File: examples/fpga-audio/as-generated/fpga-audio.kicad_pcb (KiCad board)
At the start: 2 copper layers, 100 x 84 mm, 29 parts, among them J1 3V3 IN, J2 AUDIO OUT, J3 SPI PROG, U1 iCE40UP5K, U2 PCM5102A, U3 AP2112K-1.2, U4 W25Q32JV, X1 12MHz

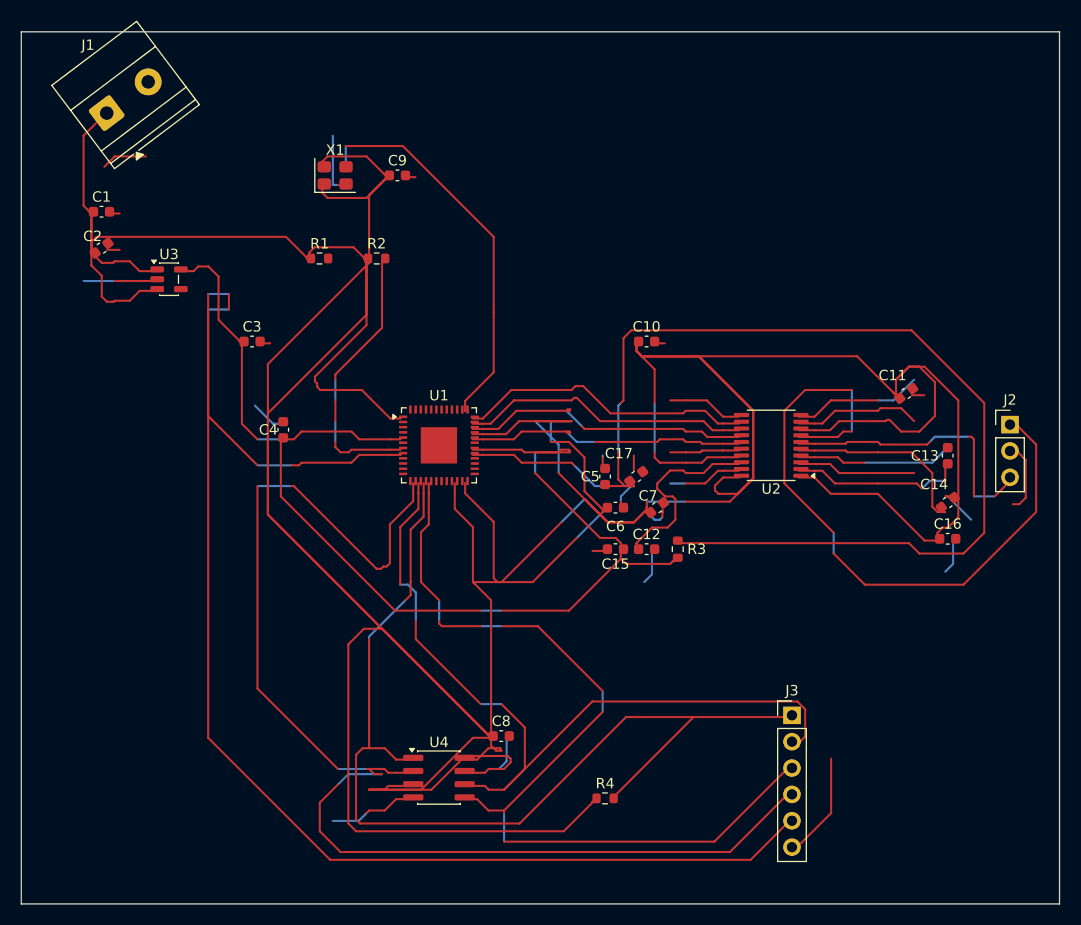
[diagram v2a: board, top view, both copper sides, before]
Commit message: Reroute the FPGA board and record what the rip-up loop bought
Eleven rip-ups and three re-orderings later, and the sixth promotion rolled
back because it left I2S_SCK with no lane:

  route.detour   VCCPLL at 5.0x   ->  gone
  route.wander   4 runs           ->  2
  acute corners  3                ->  2
  route.return_path 7 nets        ->  6
  DRC errors     1 unconnected    ->  0

Board findings 1/10/8 -> 0/9/8, and the gate goes from 5 blocking to 3. Under
KiCad's own checks the board is now clean: no DRC errors, nothing unconnected,
no schematic-parity findings.

What is left is the two-layer choice itself. Six nets run over cuts in the
back-side plane because a 48-pin QFN with no inner layer has to bring the SPI
bus out somewhere, and re-ordering cannot make a plane that is not there.
Recorded in REVIEW.md rather than waived.

All thirty example images are re-rendered. 514 tests pass on KiCad 10.0.4 and
9.0.9; ruff clean.

Co-Authored-By: Claude Opus 5 <noreply@anthropic.com>
Claude-Session: https://claude.ai/code/session_01DUj7Ltu92tWg159mCSacwY
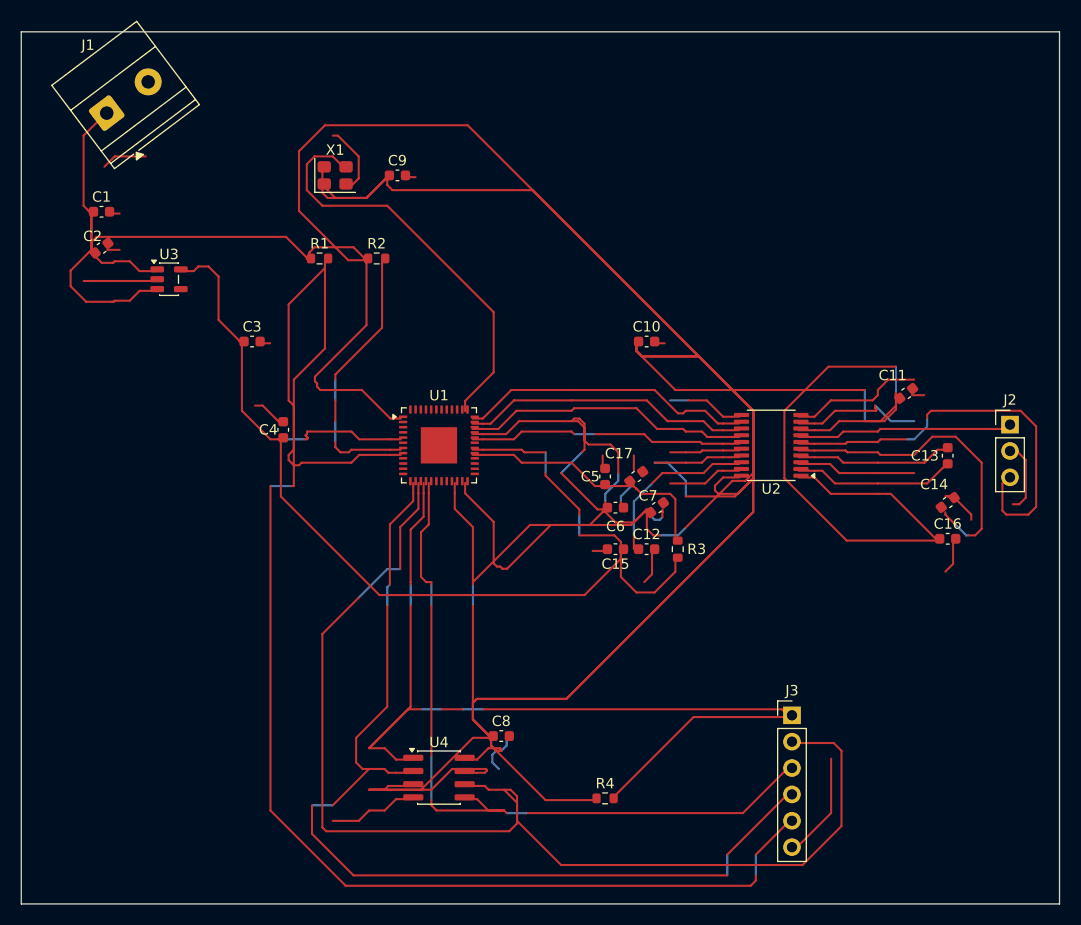
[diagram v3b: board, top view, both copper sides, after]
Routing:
- net /VCCPLL: track 113.9 -> 25.5 mm
- net +3V3: track 626.7 -> 685.2 mm
- net /OUTR: track 66.0 -> 20.6 mm
- net /SPI_SCK: track 79.1 -> 115.9 mm
- net /SPI_SO: track 122.3 -> 96.7 mm
- net /SPI_SI: track 86.4 -> 73.2 mm
- net /OUTL: track 27.2 -> 40.2 mm
- net /VNEG: track 18.5 -> 30.8 mm
- net /CRESET: track 141.8 -> 146.0 mm
- net GND: track 134.2 -> 137.6 mm
- net /SPI_SS: track 97.4 -> 94.4 mm
- net /+1V2: track 115.1 -> 112.4 mm
- net /LDOO: track 19.0 -> 16.5 mm
- net /CLK12: track 38.1 -> 40.5 mm
- net /CAPP: track 16.6 -> 15.4 mm
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
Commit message: Learn the drawing from the boards people drew
The brief for this round: relying on the autorouter and the numbers alone is
not enough - organise what pictorial correctness looks like from ordinary
circuits and open designs, and improve the drawing itself. So it starts in
KiCad's own demo corpus, measured and looked at, and ends with the habits
pushed into the generator.

tools/board_signature.py (new) reduces "looks autorouted" to five numbers.
Hand-routed two-layer boards cluster tightly: 10-47% of copper on the second
face, median segments 1.8-3.5 mm, 9-25 corners per decimetre, 91-98% of them
45s, 0.3-16 vias per decimetre. Rendering interf_u beside our boards says the
same thing in one glance: a layer has a direction, a bus travels as a bundle,
a person covers an offset with the long straight and one diagonal.

Three habits, now in the generator:

* Router.route(follow=...): cells beside a sibling net's path are discounted,
  so a bus (nets sharing a name prefix - I2S_*, SPI_*) travels as parallel
  lanes in one corridor. The discount is a fraction of a step, so it never
  buys a detour.
* _doglegged: every wiggly stretch is redrawn as the human stroke - the
  straight along the dominant direction plus one 45 - when the dogleg is
  clear, recursing into halves where a crossing blocks the whole. The op-amp
  board's median segment rose from 0.75 mm and its corner rate fell from
  38/dm; the FPGA board landed at 1.54 mm and 17.8/dm, inside the human band.
* Purposeful stitching: the 6 mm via carpet is gone. A ring at the rim, vias
  beside every back-layer crossing (where the plane is actually cut), and a
  coarse 12 mm mesh so no pour orphans. Vias/dm: buck 41 -> 18, carrier
  28 -> 13, all five inside the corpus band, pour_fragmented still silent.

Three failures the round produced and what they taught:

* pinned(): reshaping may not move copper off any point inside an own-net
  pad - the centre alone was not enough, a routed run touches off-centre and
  the ove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
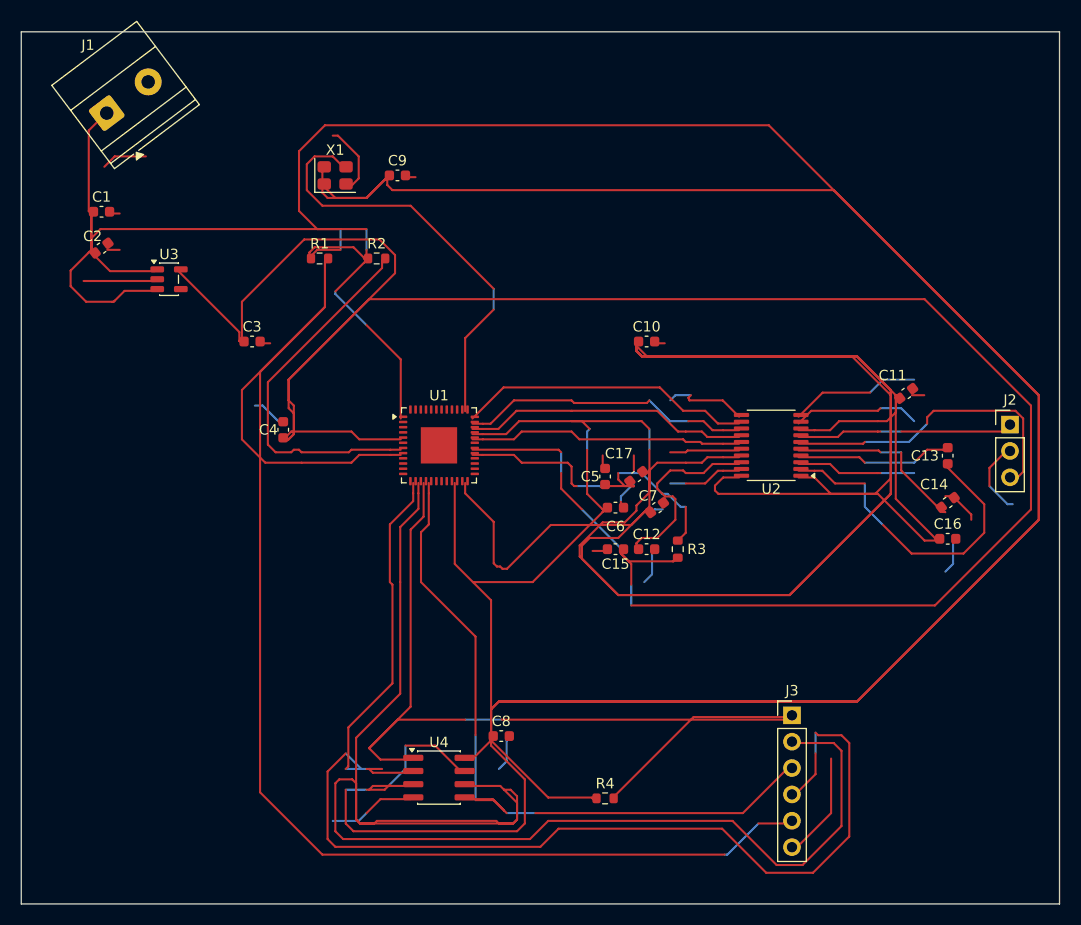
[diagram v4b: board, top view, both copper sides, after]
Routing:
- net +3V3: track 685.2 -> 905.2 mm
- net /+1V2: track 112.4 -> 237.0 mm
- net /SPI_SCK: track 115.9 -> 154.2 mm
- net /SPI_SO: track 96.7 -> 125.8 mm
- net /CAPP: track 15.4 -> 31.4 mm
- net /VNEG: track 30.8 -> 17.6 mm
- net /OUTL: track 40.2 -> 30.5 mm
- net /CDONE: track 26.5 -> 35.8 mm
- net /VCCPLL: track 25.5 -> 31.9 mm
- net /SPI_SI: track 73.2 -> 70.1 mm
- net /LDOO: track 16.5 -> 19.0 mm
- net GND: track 137.6 -> 135.9 mm
- net /CLK12: track 40.5 -> 41.8 mm

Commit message: A net may not cross its own copper
The reviewer looked at the plots, saw tracks driven through each other, and
asked whether the other checks were really passing. Both halves of the
answer were worth keeping. Measured directly - every pair of same-layer
segments on every reviewed board - there is not one crossing between
different nets: DRC reports zero errors, zero shorts, zero unconnected, and
it is not being fooled. What the plots show is a net crossing *itself*:
thirteen places on the FPGA board, one each on the op-amp and the buck.
Same potential, so DRC has nothing to say; no length ratio catches it; no
rule of ours looked. The checks were honest. The check list had a hole
exactly the shape of what the eye catches first.

route.self_crossing (new, warning, promoted by ai-generated) measures it:
two branches of one net crossing means the copper carries a redundant loop,
and a person never draws one. KiCad's demo corpus: 6 of 16 boards carry one
to three, at dense escapes.

_unlooped (new pass) is the fix, as a graph question: split every same-net
crossing so the X is a node, and while any cycle remains in the net's
copper, remove the longest junction-to-junction chain of the cycle -
connectivity is kept by definition, a cycle has two ways round, and the
amputated X becomes an ordinary corner. The clearance oracle now also
refuses to let _doglegged or _straighten draw a new X over their own net.

The cutter was wrong twice before it was right, both times the same lesson:
KiCad's connectivity is geometric, a track graph is endpoint topology, and
the difference is exactly a pad. The escape fan draws a micro-hook inside
an off-grid pad - the overlap is the connection - and the graph read it as
a dangling loop and amputated the pad's only feed. Nodes inside an own-net
pad are anchors now, a cycle wholly inside one pad is immune, and segments
passing over a pad are split so the feed is a node the cut must respect.

Self-crossings on the five reviewed boards: 0/0/0/0/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
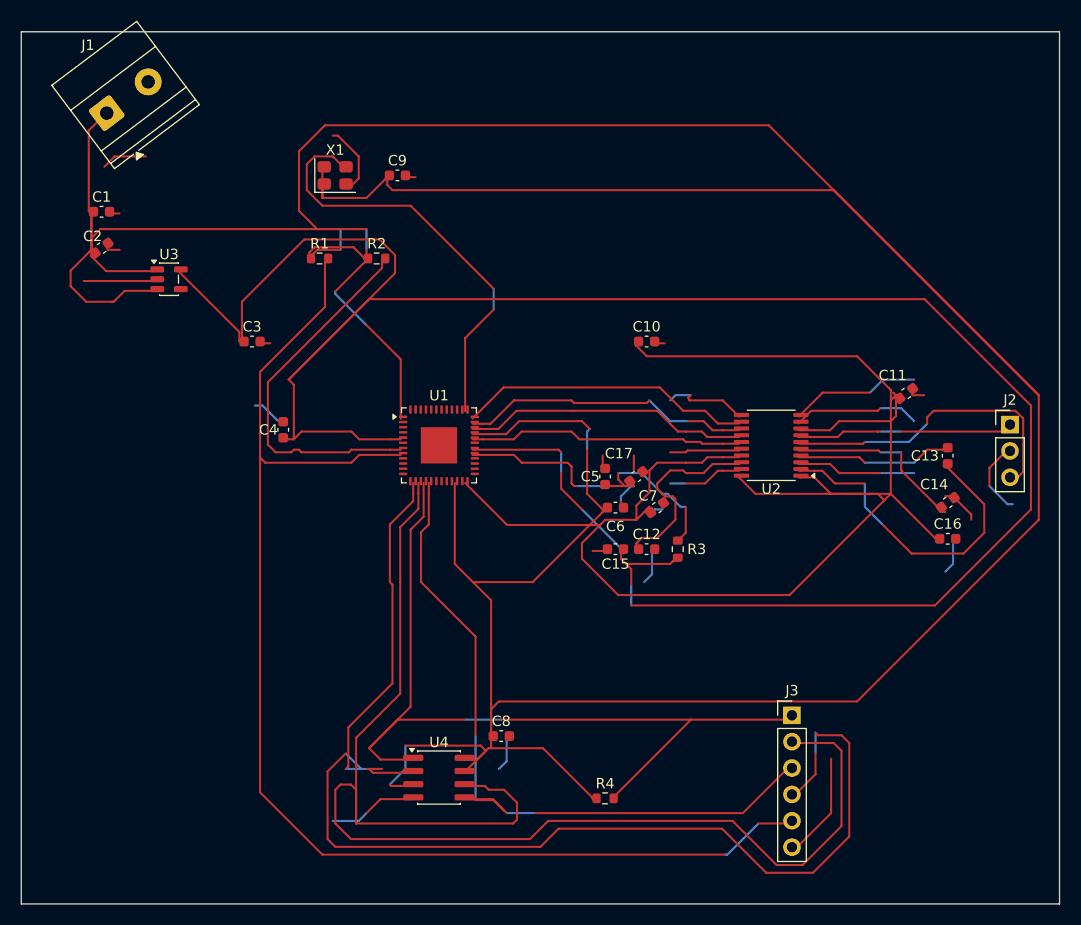
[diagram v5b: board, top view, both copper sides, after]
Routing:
- net +3V3: track 905.2 -> 602.4 mm
- net /CRESET: track 145.7 -> 122.9 mm
- net /SPI_SCK: track 154.2 -> 133.4 mm
- net /SPI_SS: track 94.3 -> 84.9 mm
- net /+1V2: track 237.0 -> 228.7 mm

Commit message: Regenerate the FPGA board on the spine, and write round twelve down
The circled cluster is gone as a class: C15 is fed by one arm, junctions
sit on the trunks, and no small pad on any board carries more than three
arms - where the hand-routed corpus sits. The board is 15% lighter in
copper (1860 mm to 1583 mm). The rails no longer wander; what the gate
still blocks on is three SPI nets over plane cuts, two signal detours and
three corners - floorplan on a QFN-48 over two layers, stated rather than
waived. REVIEW.md section 17 records the round, including the three
check_board catches it took to state one straight stroke under a QFN.

Co-Authored-By: Claude Fable 5 <noreply@anthropic.com>
Claude-Session: https://claude.ai/code/session_01DUj7Ltu92tWg159mCSacwY
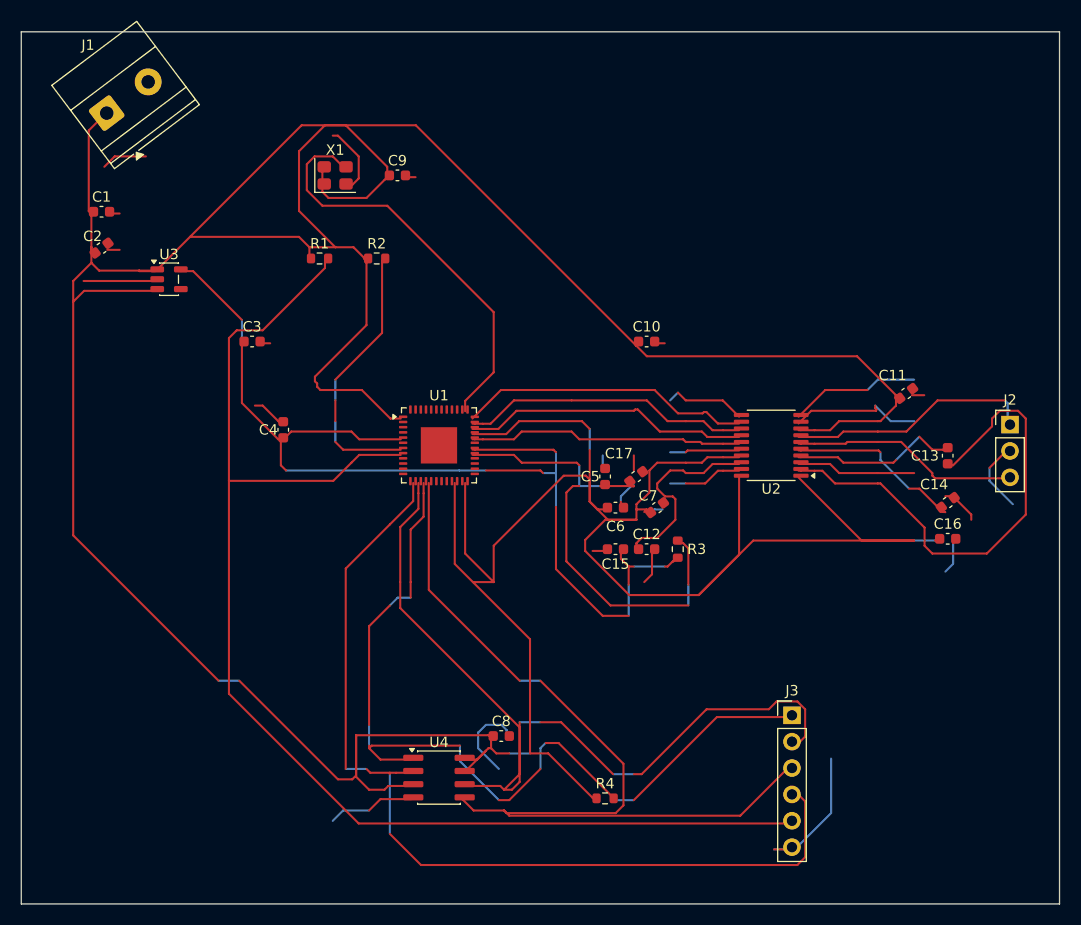
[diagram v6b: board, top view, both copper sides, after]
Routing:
- net /+1V2: track 228.7 -> 102.4 mm
- net +3V3: track 602.4 -> 489.7 mm
- net /SPI_SCK: track 133.4 -> 84.6 mm
- net /SPI_SO: track 125.8 -> 91.3 mm
- net /CAPP: track 31.4 -> 47.7 mm
- net /SPI_SI: track 70.1 -> 86.0 mm
- net /VCCPLL: track 31.8 -> 46.9 mm
- net /CDONE: track 35.8 -> 26.0 mm
- net /OUTL: track 30.5 -> 21.8 mm
- net GND: track 135.9 -> 143.9 mm
- net /OUTR: track 20.6 -> 24.0 mm
- net /CLK12: track 41.8 -> 40.5 mm
- net /SPI_SS: track 84.9 -> 86.0 mm
- net /CAPM: track 14.9 -> 15.9 mm
- net /CRESET: track 122.9 -> 123.9 mm
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
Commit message: Regenerate all five on the round-thirteen rules, and write the round down
The four fast boards pass their gates; measured across all five there are
zero crossings, zero doubled runs, zero mid-run width steps, every pour
piece over 8 mm2 holds its own via, and the shell reaches to 1.2 mm of
every edge. The FPGA sheet's two power blocks move clear of the frame -
the extended margin rule caught the second one this round. Its board
still fails, and the debt now has one name: four SPI nets at 11-20 mm
over plane cuts, two corners, and three detours all on the 3.3 V rail,
the twenty-link net that wants the same stated spine the 1.2 V rail got.
REVIEW.md section 18 records the round.

Co-Authored-By: Claude Fable 5 <noreply@anthropic.com>
Claude-Session: https://claude.ai/code/session_01DUj7Ltu92tWg159mCSacwY
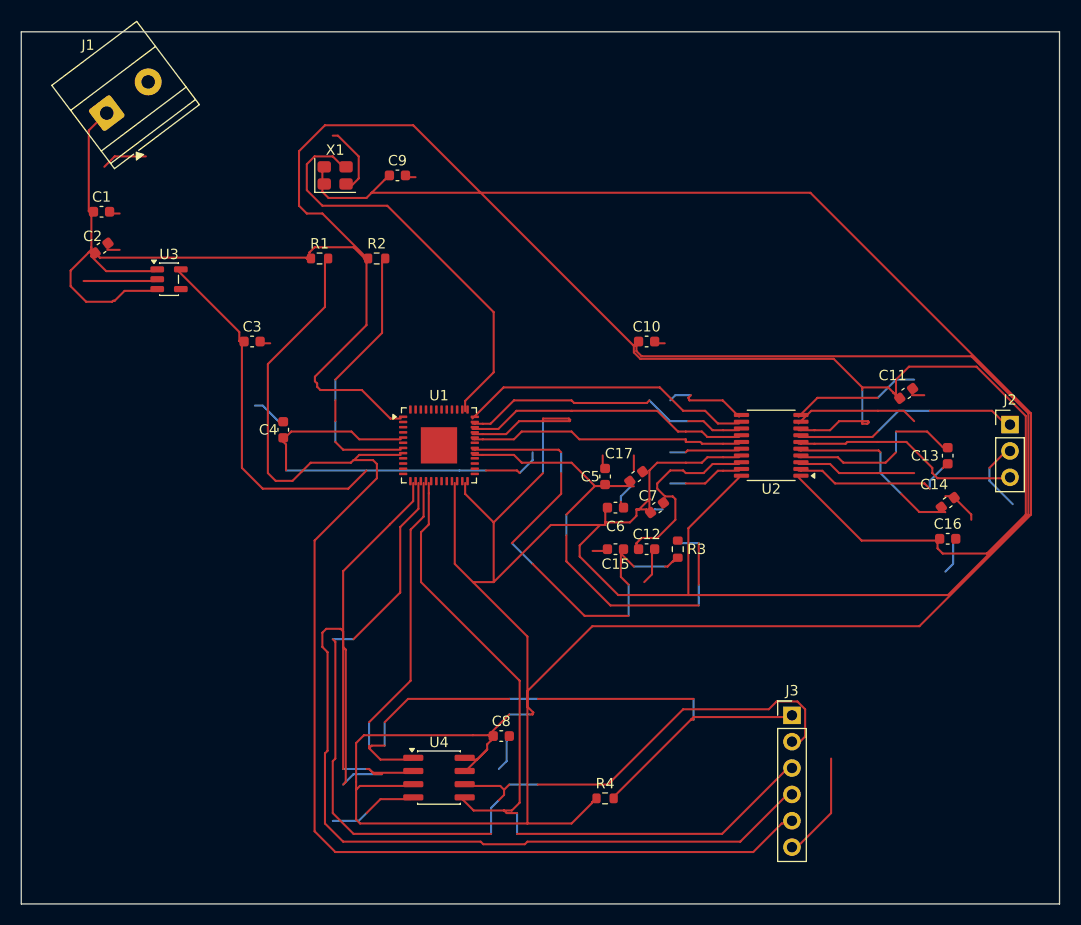
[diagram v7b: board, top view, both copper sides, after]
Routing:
- net +3V3: track 489.7 -> 670.7 mm
- net /SPI_SO: track 91.3 -> 126.1 mm
- net /CAPP: track 47.7 -> 16.2 mm
- net /+1V2: track 102.4 -> 121.9 mm
- net /SPI_SCK: track 84.6 -> 98.9 mm
- net /SPI_SI: track 86.0 -> 73.6 mm
- net GND: track 143.9 -> 135.4 mm
- net /SPI_SS: track 86.0 -> 89.5 mm
- net /OUTR: track 24.0 -> 21.8 mm
- net /CAPM: track 15.9 -> 17.5 mm
- net /VCCPLL: track 46.9 -> 48.0 mm
- net /CRESET: track 123.9 -> 124.9 mm
- net /VNEG: track 17.0 -> 17.8 mm
